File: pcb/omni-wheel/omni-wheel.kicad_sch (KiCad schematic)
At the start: 36 parts, among them IC1 AP63301WU-7, IC2 AP63301WU-7, J2 Motor2_output, J3 Motor4_output, J4 Motor3_output, J5 STLINK, J6 Motor1_output, J7 12V Input, U1 SN754410NE, U2 SN754410NE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

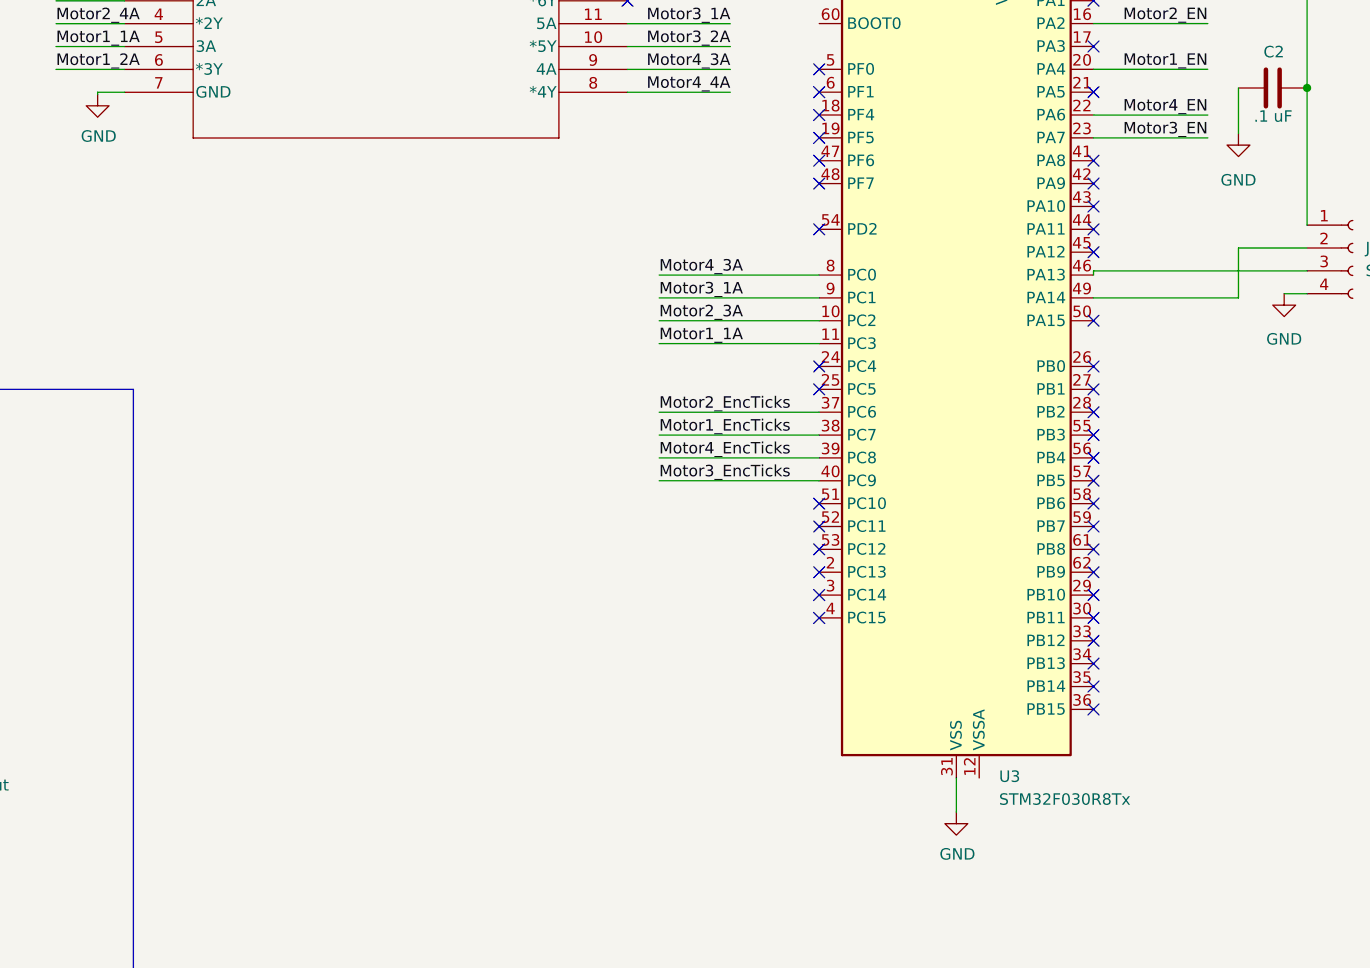
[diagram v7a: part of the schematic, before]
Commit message: Added rc uart connections, onto RPI
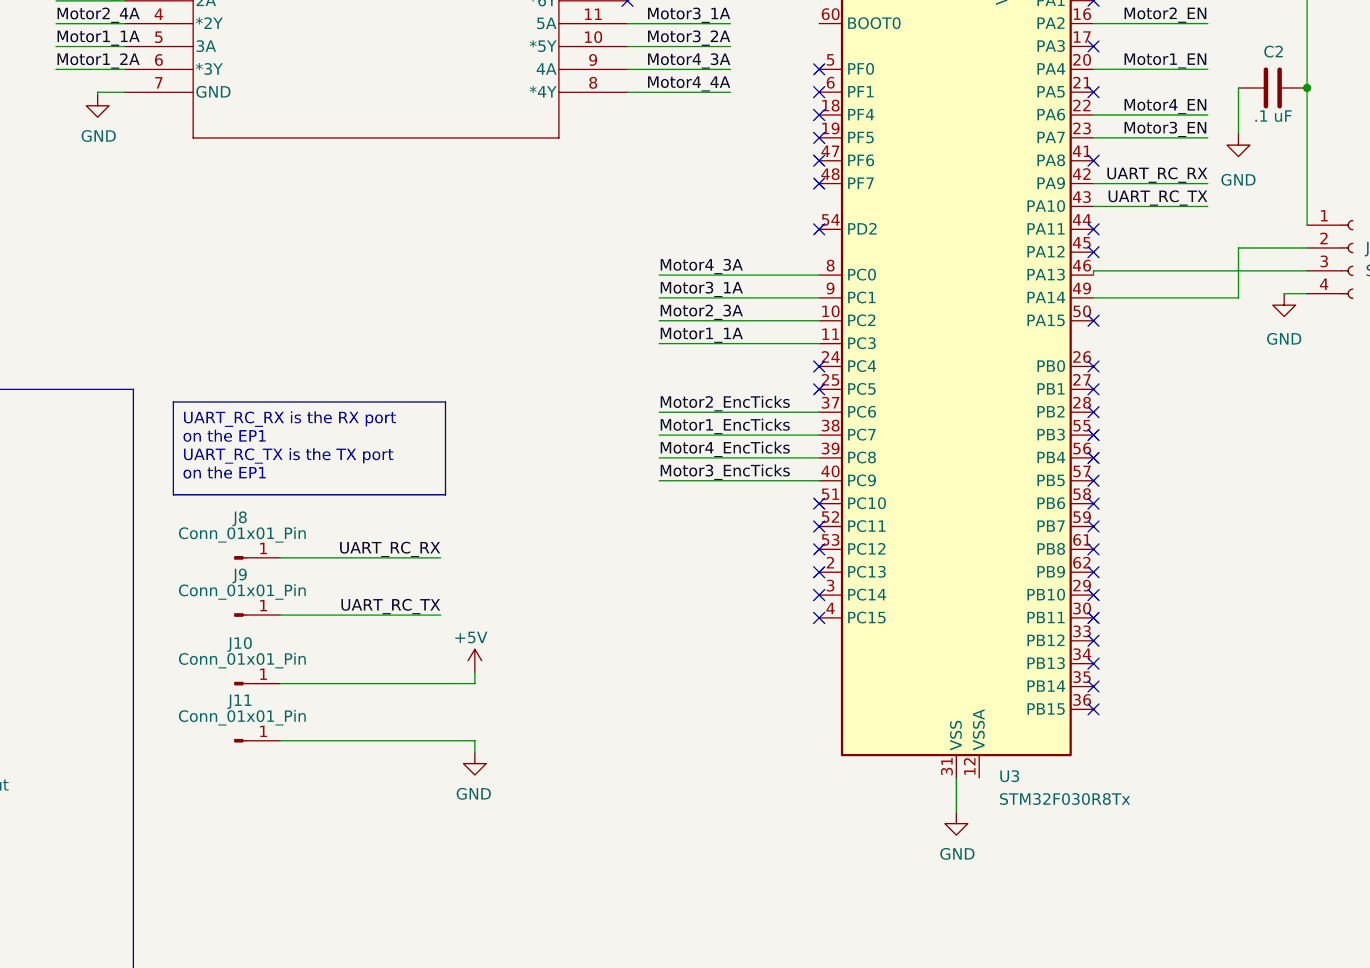
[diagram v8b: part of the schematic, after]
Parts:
- added J10, J11, J8, J9: Conn_01x01_Pin, TestPoint:TestPoint_THTPad_2.0x2.0mm_Drill1.0mm, symbol Connector:Conn_01x01_Pin
- J5: footprint (none) -> Connector_PinHeader_1.00mm:PinHeader_1x04_P1.00mm_Vertical
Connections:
- net +5V: now also J10.1 (Pin_1)
- net GND: now also J11.1 (Pin_1)
- net UART_RC_RX: now reaches U3.42 (PA9)
- net UART_RC_RX: now also J8.1 (Pin_1)
- net UART_RC_TX: now reaches U3.43 (PA10)
- net UART_RC_TX: now also J9.1 (Pin_1)
- no-connect marks 45 -> 43
